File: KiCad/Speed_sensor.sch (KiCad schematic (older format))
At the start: 45 parts

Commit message: updated battery charging with Manus chip, added low frequency crystal
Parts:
- removed C? (x2): 1u, symbol Device:C_Small
- removed H?: LiPo+, symbol Mechanical:MountingHole_Pad
- removed H?: LiPo-, symbol Mechanical:MountingHole_Pad
- removed U?: MCP73811T-420I-OT, Package_TO_SOT_SMD:SOT-23-5, symbol Battery_Management:MCP73811T-420I-OT
- added C? (x2): 1u, symbol Device:C_Small
- added C? (x2): 12p, symbol Device:C_Small
- added C?: 0,8p, symbol Device:C_Small
- added D?: IN, symbol Device:LED_Small
- added D?: charging, symbol Device:LED_Small
- added H?: LiPo+, symbol Mechanical:MountingHole_Pad
- added H?: LiPo-, symbol Mechanical:MountingHole_Pad
- added L?: 3,9n, symbol Device:L_Small
- added R?: 10,8k, symbol Device:R_Small
- added R?: 10k, symbol Device:R_Small
- added R? (x2): 1,5k, symbol Device:R_Small
- added U?: BQ24040DSQR, symbol Nils_KiCADLibrary:BQ24040DSQR
- added Y?: 32,768kHz, symbol Device:Crystal_Small
- C?: value 100p -> N.C.
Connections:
- net +5V: now also C?.1, U?.1 (IN)
- net +BATT: now also C?.1, H?.1, R?.2, R?.2, U?.10 (OUT)
- net ANT: now also L?.1; no longer U?.30 (ANT)
- net GND: now also C?.1, C?.2, C?.2, C?.2, C?.2, H?.1, R?.1, R?.2, U?.3 (VSS), U?.7 (ISET2)
- net XL1: now reaches U?.2 (P0.00/XL1)
- net XL1: now also C?.1, Y?.1
- net XL2: now reaches U?.3 (P0.01/XL2)
- net XL2: now also C?.1, Y?.2
- net AIN0: now reaches U?.4 (P0.02/AIN0)
- net AIN1: now reaches U?.5 (P0.03/AIN1)
- net AIN2: now reaches U?.6 (P0.04/AIN2)
- net AIN3: now reaches U?.7 (P0.05/AIN3)
- new net: C?.2, L?.2, U?.30 (ANT)
- new net: D?.2 (A), R?.1 (x2)
- new net BQ_ISET: R?.1, U?.2 (ISET)
- new net BQ_TS: R?.2, U?.9 (TS)
- new net ~BQ_CHG~: D?.1 (K), U?.8 (~CHG~)
- new net ~BQ_PG~: D?.1 (K), U?.5 (~PG~)
- no-connect marks 8 -> 10
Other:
- note added: "AIN0-3 werden erstmal nicht verwenden, \nsollten aber mit pads versehen werden \num flexibel Analoge Inputs zu ermöglichen."
- note added: "Hier noch was zum Schutz\nvor falscher Polarisierung\neinbauen (direkt an + Akkuanschluss)"
- note added: "PRETERM left floating: internally sets \ntermination and pre-charge to 10/20% \nof fast charge current respectively"
- note removed: "Hier noch was zum Schutz\nvor falscher Polarisierung\neinbauen"
- note removed: "den hier brauch ich!"
- moved on the sheet: BMA?, C?, D?, H?, J?, L?, R?, U?, Y?

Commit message: switch to Manus Accelerometer, switch back to A4 page size
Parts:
- removed BMA?: BMA423-ds004-00, symbol Nils_KiCADLibrary:BMA423-ds004-00
- removed C? (x2): 100n, symbol Device:C_Small
- added C?: 100n, symbol Device:C_Small
- added C?: 10u, symbol Device:C_Small
- added U?: LIS2DH12, symbol Nils_KiCADLibrary:LIS2DH12
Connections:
- net +3V0: now also C?.1, C?.1, U?.10 (Vdd_IO), U?.9 (Vdd)
- net GND: now also C?.2, C?.2, U?.5 (RES), U?.6 (GND), U?.7 (GND), U?.8 (GND)
- net BMA_INT1 renamed ACCEL_INT2
- net ACCEL_INT2: now also U?.11 (INT2)
- net BMA_INT2 renamed ACCEL_INT1
- net ACCEL_INT1: now also U?.12 (INT1)
- net SPI_01_CSB renamed SPI_01_CS
- net SPI_01_CS: now also U?.2 (CS)
- net SPI_01_MISO renamed SPI_MISO
- net SPI_MISO: now also U?.3 (SDO/SA0)
- net SPI_01_MOSI renamed SPI_MOSI
- net SPI_MOSI: now also U?.4 (SDA/SDI/SDO)
- net SPI_01_SCK renamed SPI_SCK
- net SPI_SCK: now also U?.1 (SCL/SPC)
- no-connect marks 10 -> 8
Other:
- moved on the sheet: C?, D?, H?, J?, L?, R?, U?, Y?

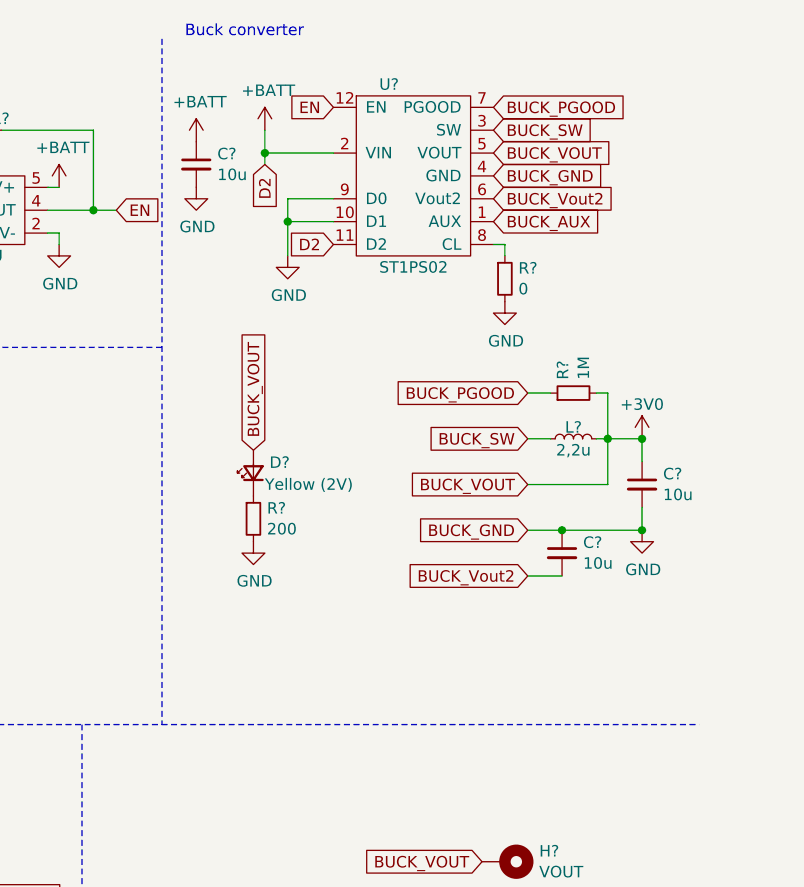
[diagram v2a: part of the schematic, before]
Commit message: buck converter circuit made more readable
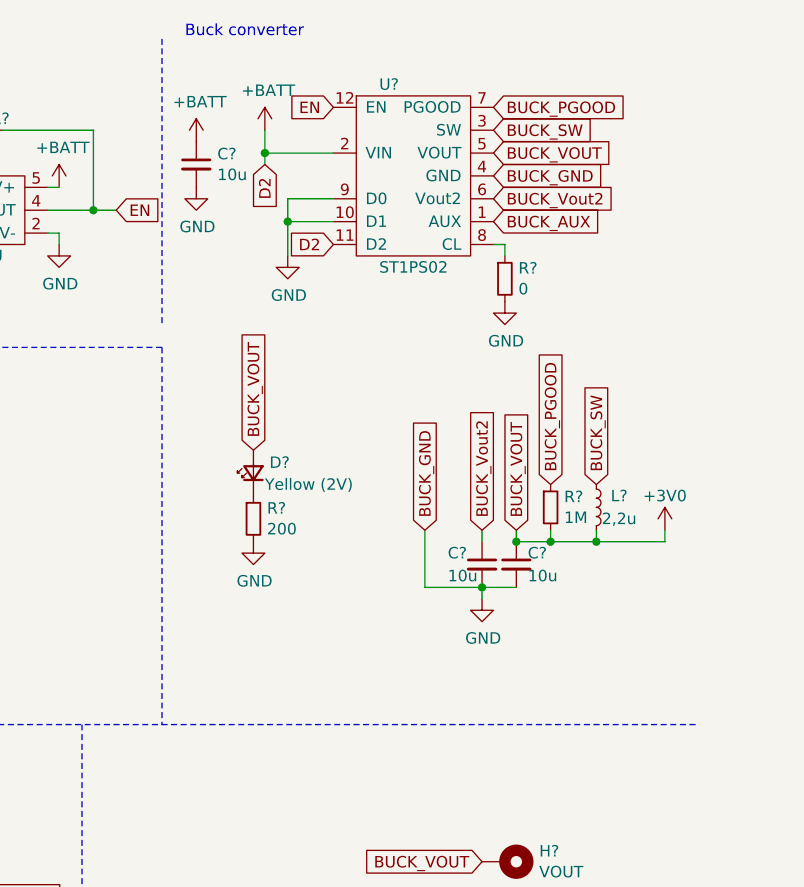
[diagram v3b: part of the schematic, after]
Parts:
- removed C? (x2): 10u, symbol Device:C_Small
- removed L?: 2,2u, symbol Device:L_Small
- removed R?: 1M, symbol Device:R_Small
- added C? (x2): 10u, symbol Device:C_Small
- added L?: 2,2u, symbol Device:L_Small
- added R?: 1M, symbol Device:R_Small
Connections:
- net +3V0: now also C?.1, L?.2, R?.2
- net BUCK_PGOOD: now also R?.1
- net BUCK_SW: now also L?.1
- net BUCK_Vout2: now also C?.1
- net GND: now also C?.2, C?.2
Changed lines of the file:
@@
 Wire Wire Line
 	10350 1500 10300 1500
-Text GLabel 10450 2150 0    50   Input ~ 0
-BUCK_PGOOD
-Text GLabel 10450 2350 0    50   Input ~ 0
-BUCK_SW
-Text GLabel 10450 2550 0    50   Input ~ 0
-BUCK_VOUT
-Text GLabel 10450 2750 0    50   Input ~ 0
-BUCK_GND
-Text GLabel 10450 2950 0    50   Input ~ 0
-BUCK_Vout2
-$Comp
-L Device:R_Small R?
-U 1 1 60A8A44F
-P 10650 2150
-AR Path="/608A57BF/60A8A44F" Ref="R?"  Part="1"
-AR Path="/60A8A44F" Ref="R?"  Part="1"
-F 0 "R?" H 10709 2196 50  0000 L CNN
-F 1 "1M" H 10709 2105 50  0000 L CNN
-F 2 "" H 10650 2150 50  0001 C CNN
-F 3 "~" H 10650 2150 50  0001 C CNN
-	1    10650 2150
-	0    -1   -1   0
-$EndComp
-$Comp
-L Device:C_Small C?
-U 1 1 60A8A886
-P 10950 2550
-AR Path="/608A57BF/60A8A886" Ref="C?"  Part="1"
-AR Path="/60A8A886" Ref="C?"  Part="1"
-F 0 "C?" H 11042 2596 50  0000 L CNN
-F 1 "10u" H 11042 2505 50  0000 L CNN
-F 2 "" H 10950 2550 50  0001 C CNN
-F 3 "~" H 10950 2550 50  0001 C CNN
-	1    10950 2550
-	1    0    0    -1
-$EndComp
-$Comp
-L Device:C_Small C?
-U 1 1 60A8ACD6
-P 10600 2850
-AR Path="/608A57BF/60A8ACD6" Ref="C?"  Part="1"
-AR Path="/60A8ACD6" Ref="C?"  Part="1"
-F 0 "C?" H 10692 2896 50  0000 L CNN
-F 1 "10u" H 10692 2805 50  0000 L CNN
-F 2 "" H 10600 2850 50  0001 C CNN
-F 3 "~" H 10600 2850 50  0001 C CNN
-	1    10600 2850
-	1    0    0    -1
-$EndComp
-$Comp
-L Device:L_Small L?
-U 1 1 60A8B1B5
-P 10650 2350
-F 0 "L?" V 10700 2350 50  0000 C CNN
-F 1 "2,2u" V 10600 2350 50  0000 C CNN
-F 2 "" H 10650 2350 50  0001 C CNN
-F 3 "~" H 10650 2350 50  0001 C CNN
-	1    10650 2350
-	0    -1   -1   0
-$EndComp
-Wire Wire Line
-	10550 2350 10450 2350
-Wire Wire Line
-	10800 2350 10750 2350
-$Comp
-L power:GND #PWR?
-U 1 1 60AA1F3D
-P 10950 2750
-AR Path="/608A57BF/60AA1F3D" Ref="#PWR?"  Part="1"
-AR Path="/60AA1F3D" Ref="#PWR?"  Part="1"
-F 0 "#PWR?" H 10950 2500 50  0001 C CNN
-F 1 "GND" H 10955 2577 50  0000 C CNN
-F 2 "" H 10950 2750 50  0001 C CNN
-F 3 "" H 10950 2750 50  0001 C CNN
-	1    10950 2750
-	1    0    0    -1
-$EndComp
-Wire Wire Line
-	10450 2550 10800 2550
-Wire Wire Line
-	10800 2550 10800 2350
-Connection ~ 10800 2350
-Wire Wire Line
-	10800 2350 10950 2350
-Wire Wire Line
-	10950 2350 10950 2450
-Wire Wire Line
-	10600 2950 10450 2950
-Wire Wire Line
-	10450 2750 10600 2750
-Wire Wire Line
-	10600 2750 10950 2750
-Wire Wire Line
-	10950 2750 10950 2650
-Connection ~ 10600 2750
-Connection ~ 10950 2750
-Wire Wire Line
-	10450 2150 10550 2150
-Wire Wire Line
-	10750 2150 10800 2150
-Wire Wire Line
-	10800 2150 10800 2350
-$Comp
-L power:+3V0 #PWR?
-U 1 1 60B121B5
-P 10950 2350
-F 0 "#PWR?" H 10950 2200 50  0001 C CNN
-F 1 "+3V0" H 10950 2500 50  0000 C CNN
-F 2 "" H 10950 2350 50  0001 C CNN
-F 3 "" H 10950 2350 50  0001 C CNN
-	1    10950 2350
-	1    0    0    -1
-$EndComp
-Connection ~ 10950 2350
 Wire Wire Line
 	3150 3100 3150 4150
@@
 	5950 3600 11200 3600
 Wire Notes Line
-	8850 600  8850 3600
-Wire Notes Line
 	8850 1950 500  1950
 Wire Notes Line
@@
 Wire Notes Line
 	8500 5200 5950 5200
+Wire Notes Line
+	8850 1950 8850 3600
+Wire Notes Line
+	8850 600  8850 1850
+Text GLabel 10550 2550 1    50   Input ~ 0
+BUCK_PGOOD
+Text GLabel 10750 2550 1    50   Input ~ 0
+BUCK_SW
+Text GLabel 10400 2750 1    50   Input ~ 0
+BUCK_VOUT
+Text GLabel 10000 2750 1    50   Input ~ 0
+BUCK_GND
+Text GLabel 10250 2750 1    50   Input ~ 0
+BUCK_Vout2
+$Comp
+L Device:C_Small C?
+U 1 1 60C8F999
+P 10400 2900
+AR Path="/608A57BF/60C8F999" Ref="C?"  Part="1"
+AR Path="/60C8F999" Ref="C?"  Part="1"
+F 0 "C?" H 10450 2950 50  0000 L CNN
+F 1 "10u" H 10450 2850 50  0000 L CNN
+F 2 "" H 10400 2900 50  0001 C CNN
+F 3 "~" H 10400 2900 50  0001 C CNN
+	1    10400 2900
+	1    0    0    -1
+$EndComp
+$Comp
+L Device:C_Small C?
+U 1 1 60C90235
+P 10250 2900
+AR Path="/608A57BF/60C90235" Ref="C?"  Part="1"
+AR Path="/60C90235" Ref="C?"  Part="1"
+F 0 "C?" H 10100 2950 50  0000 L CNN
+F 1 "10u" H 10100 2850 50  0000 L CNN
+F 2 "" H 10250 2900 50  0001 C CNN
+F 3 "~" H 10250 2900 50  0001 C CNN
+	1    10250 2900
+	1    0    0    -1
+$EndComp
+Wire Wire Line
+	10250 2750 10250 2800
+Wire Wire Line
+	10400 2750 10400 2800
+$Comp
+L power:GND #PWR?
+U 1 1 60CA0A68
+P 10250 3050
+AR Path="/608A57BF/60CA0A68" Ref="#PWR?"  Part="1"
+AR Path="/60CA0A68" Ref="#PWR?"  Part="1"
+F 0 "#PWR?" H 10250 2800 50  0001 C CNN
+F 1 "GND" H 10255 2877 50  0000 C CNN
+F 2 "" H 10250 3050 50  0001 C CNN
+F 3 "" H 10250 3050 50  0001 C CNN
+	1    10250 3050
+	1    0    0    -1
+$EndComp
+Wire Wire Line
+	10250 3050 10250 3000
+Wire Wire Line
+	10400 3000 10250 3000
+Connection ~ 10250 3000
+$Comp
+L power:+3V0 #PWR?
+U 1 1 60CABFF4
+P 11050 2750
+F 0 "#PWR?" H 11050 2600 50  0001 C CNN
+F 1 "+3V0" H 11050 2900 50  0000 C CNN
+F 2 "" H 11050 2750 50  0001 C CNN
+F 3 "" H 11050 2750 50  0001 C CNN
+	1    11050 2750
+	1    0    0    -1
+$EndComp
+Wire Wire Line
+	11050 2750 11050 2800
+Connection ~ 10400 2800
+Wire Wire Line
+	10000 2750 10000 3000
+Wire Wire Line
+	10000 3000 10250 3000
+$Comp
+L Device:L_Small L?
+U 1 1 60CCE7A3
+P 10750 2650
+F 0 "L?" H 10850 2700 50  0000 C CNN
+F 1 "2,2u" H 10850 2600 50  0000 C CNN
+F 2 "" H 10750 2650 50  0001 C CNN
+F 3 "~" H 10750 2650 50  0001 C CNN
+	1    10750 2650
+	1    0    0    -1
+$EndComp
+$Comp
+L Device:R_Small R?
+U 1 1 60CDA7DE
+P 10550 2650
+AR Path="/608A57BF/60CDA7DE" Ref="R?"  Part="1"
+AR Path="/60CDA7DE" Ref="R?"  Part="1"
+F 0 "R?" H 10609 2696 50  0000 L CNN
+F 1 "1M" H 10609 2605 50  0000 L CNN
+F 2 "" H 10550 2650 50  0001 C CNN
+F 3 "~" H 10550 2650 50  0001 C CNN
+	1    10550 2650
+	1    0    0    -1
+$EndComp
+Wire Wire Line
+	10750 2750 10750 2800
+Wire Wire Line
+	10550 2750 10550 2800
+Wire Wire Line
+	10400 2800 10550 2800
+Connection ~ 10550 2800
+Connection ~ 10750 2800
+Wire Wire Line
+	10550 2800 10750 2800
+Wire Wire Line
+	10750 2800 11050 2800
 $EndSCHEMATC
